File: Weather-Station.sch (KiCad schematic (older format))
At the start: 62 parts

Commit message: Annotate schematic
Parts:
- gave numbers to parts that had none: 62

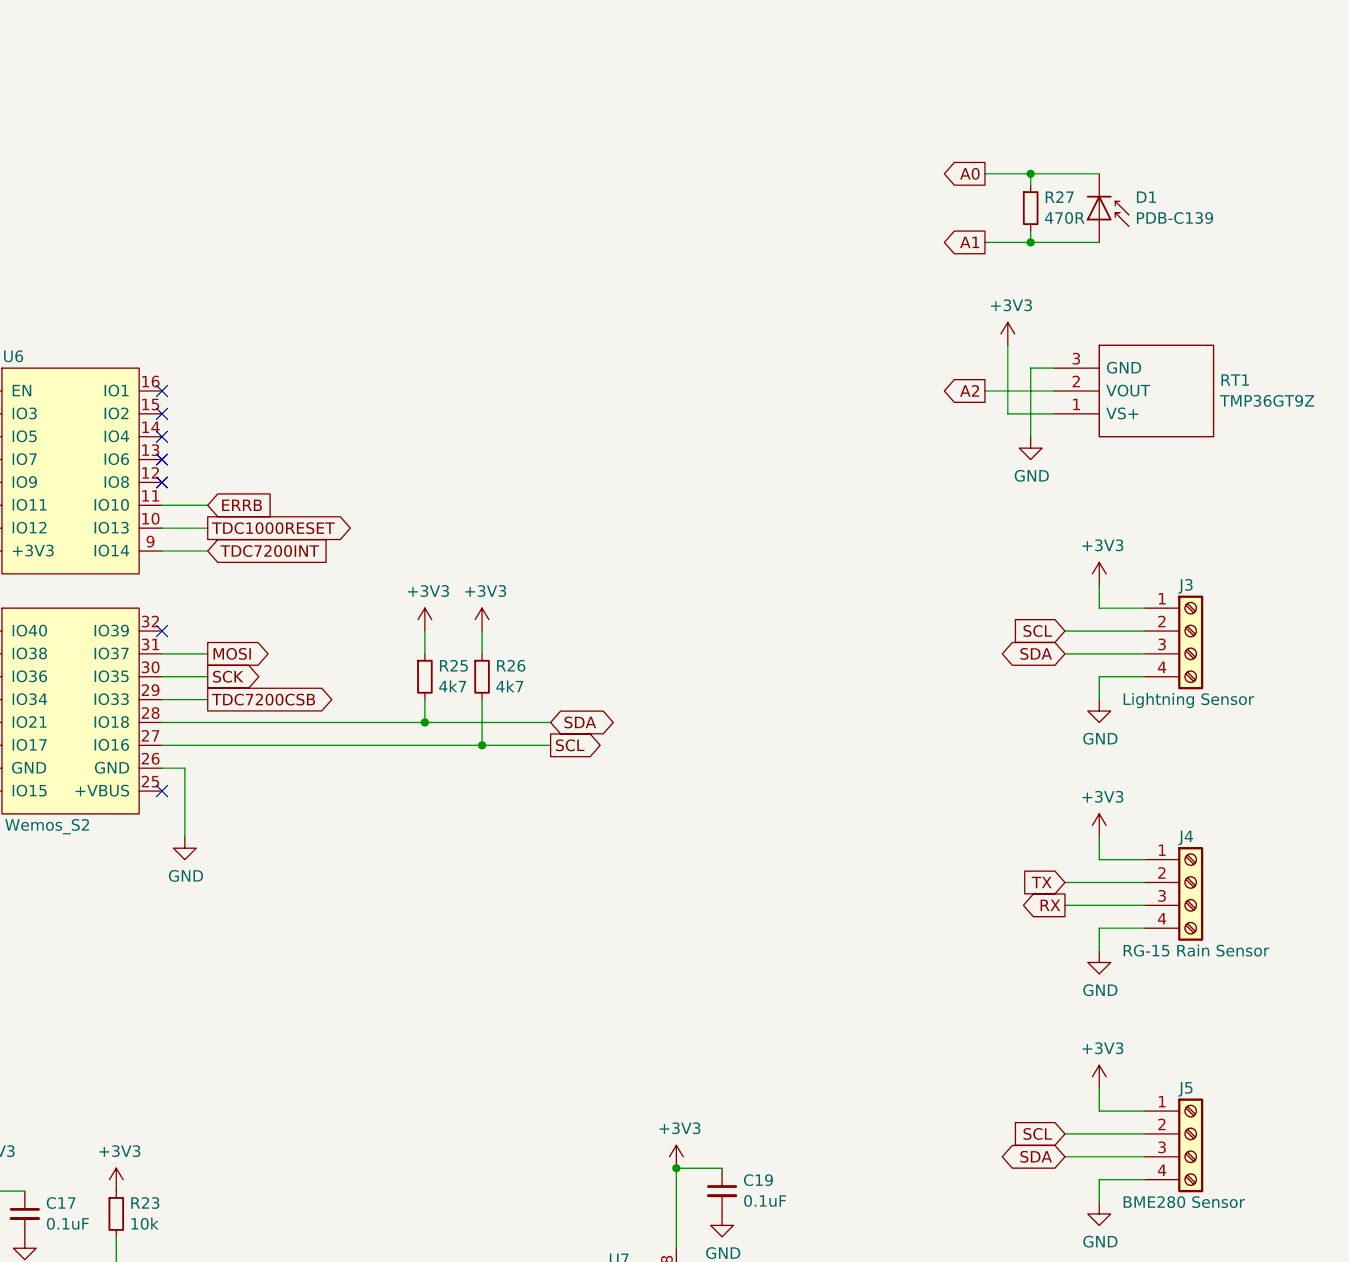
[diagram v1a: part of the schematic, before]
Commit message: Added pullups to ERRB & TDC2000INT, screw terminals for sensors.
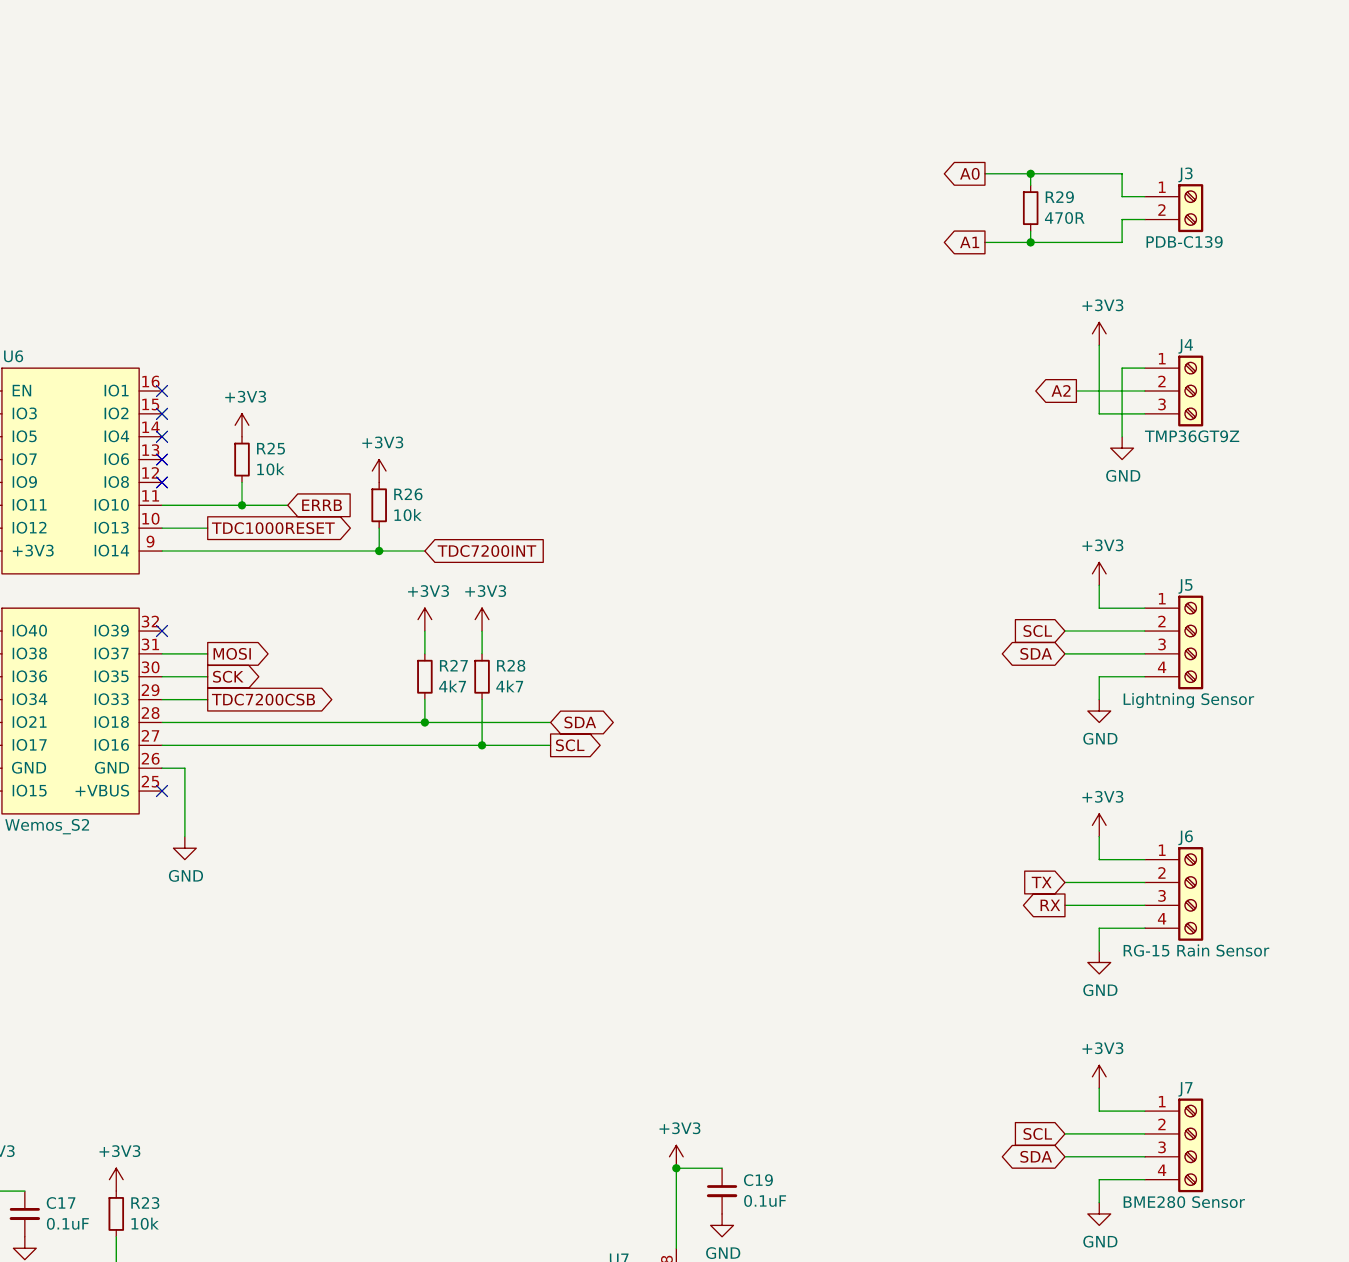
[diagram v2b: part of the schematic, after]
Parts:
- removed D1: PDB-C139, symbol Device:D_Photo
- removed RT1: TMP36GT9Z, TO-92, symbol TMP36GT9Z:TMP36GT9Z
- added J3: PDB-C139, TerminalBlock:TerminalBlock_bornier-2_P5.08mm, symbol Connector:Screw_Terminal_01x02
- added J4: TMP36GT9Z, TerminalBlock:TerminalBlock_bornier-3_P5.08mm, symbol Connector:Screw_Terminal_01x03
- added R25, R26: 10k, Resistor_SMD:R_0805_2012Metric, symbol Device:R_Small
- renumbered J3 to J5, J4 to J6, J5 to J7, R25 to R27, R26 to R28, R27 to R29
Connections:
- net +3V3: now also J4.3 (Pin_3), R25.1, R26.1
- net A0: now also J3.1 (Pin_1)
- net A1: now also J3.2 (Pin_2)
- net A2: now also J4.2 (Pin_2)
- net ERRB: now also R25.2
- net GND: now also J4.1 (Pin_1)
- net TDC7200INT: now also R26.2

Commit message: Start of PCB layout
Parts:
- J1: footprint (none) -> TerminalBlock:TerminalBlock_bornier-2_P5.08mm
- J2: footprint (none) -> TerminalBlock_Phoenix:TerminalBlock_Phoenix_MKDS-1,5-12-5.08_1x12_P5.08mm_Horizontal
- U6: footprint (none) -> ESP32:WEMOS_S2
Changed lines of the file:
@@
 F 0 "J2" H 1300 6650 50  0000 C CNN
 F 1 "Screw_Terminal_01x12" H 1218 6676 50  0001 C CNN
-F 2 "" H 1300 6050 50  0001 C CNN
+F 2 "TerminalBlock_Phoenix:TerminalBlock_Phoenix_MKDS-1,5-12-5.08_1x12_P5.08mm_Horizontal" H 1300 6050 50  0001 C CNN
 F 3 "~" H 1300 6050 50  0001 C CNN
 	1    1300 6050
@@
 F 0 "J1" H 1300 1400 50  0000 C CNN
 F 1 "PV IN" H 1250 1100 50  0000 C CNN
-F 2 "" H 1300 1300 50  0001 C CNN
+F 2 "TerminalBlock:TerminalBlock_bornier-2_P5.08mm" H 1300 1300 50  0001 C CNN
 F 3 "~" H 1300 1300 50  0001 C CNN
 	1    1300 1300
@@
 F 0 "U6" H 9450 3250 50  0000 C CNN
 F 1 "Wemos_S2" H 9600 1200 50  0000 C CNN
-F 2 "" H 9400 3150 50  0001 C CNN
+F 2 "ESP32:WEMOS_S2" H 9400 3150 50  0001 C CNN
 F 3 "" H 9400 3150 50  0001 C CNN
 	1    9400 3200

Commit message: more pcb layout
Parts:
- removed J2: Screw_Terminal_01x12, TerminalBlock_Phoenix:TerminalBlock_Phoenix_MKDS-1,5-12-5.08_1x12_P5.08mm_Horizontal, symbol Connector:Screw_Terminal_01x12
- added J2: TX1, TerminalBlock:TerminalBlock_bornier-2_P5.08mm, symbol Connector:Screw_Terminal_01x02
- added J3: TX2, TerminalBlock:TerminalBlock_bornier-2_P5.08mm, symbol Connector:Screw_Terminal_01x02
- added J4: RX1, TerminalBlock:TerminalBlock_bornier-2_P5.08mm, symbol Connector:Screw_Terminal_01x02
- added J5: RX2, TerminalBlock:TerminalBlock_bornier-2_P5.08mm, symbol Connector:Screw_Terminal_01x02
- added J6: RTD1, TerminalBlock:TerminalBlock_bornier-2_P5.08mm, symbol Connector:Screw_Terminal_01x02
- added J7: RTD2, TerminalBlock:TerminalBlock_bornier-2_P5.08mm, symbol Connector:Screw_Terminal_01x02
- renumbered J5 to J10, J6 to J11, J7 to J12, J3 to J8, J4 to J9, IC1 to U2, U2 to U3, U3 to U4, U4 to U5, U5 to U6, U6 to U7, U7 to U8
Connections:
- net GND: now also J2.2 (Pin_2), J3.2 (Pin_2), J4.2 (Pin_2), J5.2 (Pin_2), J6.2 (Pin_2), J7.2 (Pin_2)
- net RTD1: now also J6.1 (Pin_1)
- net RTD2: now also J7.1 (Pin_1)
- net TX1: now also R7.1; no longer R5.1
- net TX2: now also R5.1; no longer R7.1
- net at R5.2: now also J3.1 (Pin_1)
- net at R7.2: now also J2.1 (Pin_1)
- net at C1.2: now also J4.1 (Pin_1)
- net at C2.2: now also J5.1 (Pin_1)
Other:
- moved on the sheet: C1, C2, R5, R7
